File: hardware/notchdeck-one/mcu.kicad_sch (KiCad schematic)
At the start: 10 parts, among them J3 SWD, J4 TC2030_NL, U1 E73-2G4M08S1C

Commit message: Add schematic wiring notes support
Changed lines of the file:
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@@
 		(instances
 			(project "notchdeck-one"
-				(path "/9b1c0f7a-1d2e-4a3b-8c5d-0e6f7a8b9c01/0d4eb303-8502-4a0e-80b0-eb5483675459"
+				(path "/9b1c0f7a-1d2e-4a3b-8c5d-0e6f7a8b9c01/69c9301a-7d1c-4dfc-8a82-adc2c5ab1b11"
 					(reference "U1")
 					(unit 1)
@@
 		(instances
 			(project "notchdeck-one"
-				(path "/9b1c0f7a-1d2e-4a3b-8c5d-0e6f7a8b9c01/0d4eb303-8502-4a0e-80b0-eb5483675459"
+				(path "/9b1c0f7a-1d2e-4a3b-8c5d-0e6f7a8b9c01/69c9301a-7d1c-4dfc-8a82-adc2c5ab1b11"
 					(reference "J3")
 					(unit 1)
@@
 		(instances
 			(project "notchdeck-one"
-				(path "/9b1c0f7a-1d2e-4a3b-8c5d-0e6f7a8b9c01/0d4eb303-8502-4a0e-80b0-eb5483675459"
+				(path "/9b1c0f7a-1d2e-4a3b-8c5d-0e6f7a8b9c01/69c9301a-7d1c-4dfc-8a82-adc2c5ab1b11"
 					(reference "J4")
 					(unit 1)
@@
 		(instances
 			(project "notchdeck-one"
-				(path "/9b1c0f7a-1d2e-4a3b-8c5d-0e6f7a8b9c01/0d4eb303-8502-4a0e-80b0-eb5483675459"
+				(path "/9b1c0f7a-1d2e-4a3b-8c5d-0e6f7a8b9c01/69c9301a-7d1c-4dfc-8a82-adc2c5ab1b11"
 					(reference "C1")
 					(unit 1)
@@
 		(instances
 			(project "notchdeck-one"
-				(path "/9b1c0f7a-1d2e-4a3b-8c5d-0e6f7a8b9c01/0d4eb303-8502-4a0e-80b0-eb5483675459"
+				(path "/9b1c0f7a-1d2e-4a3b-8c5d-0e6f7a8b9c01/69c9301a-7d1c-4dfc-8a82-adc2c5ab1b11"
 					(reference "C2")
 					(unit 1)
@@
 		(instances
 			(project "notchdeck-one"
-				(path "/9b1c0f7a-1d2e-4a3b-8c5d-0e6f7a8b9c01/0d4eb303-8502-4a0e-80b0-eb5483675459"
+				(path "/9b1c0f7a-1d2e-4a3b-8c5d-0e6f7a8b9c01/69c9301a-7d1c-4dfc-8a82-adc2c5ab1b11"
 					(reference "C3")
 					(unit 1)
@@
 		(instances
 			(project "notchdeck-one"
-				(path "/9b1c0f7a-1d2e-4a3b-8c5d-0e6f7a8b9c01/0d4eb303-8502-4a0e-80b0-eb5483675459"
+				(path "/9b1c0f7a-1d2e-4a3b-8c5d-0e6f7a8b9c01/69c9301a-7d1c-4dfc-8a82-adc2c5ab1b11"
 					(reference "C4")
 					(unit 1)
@@
 		(instances
 			(project "notchdeck-one"
-				(path "/9b1c0f7a-1d2e-4a3b-8c5d-0e6f7a8b9c01/0d4eb303-8502-4a0e-80b0-eb5483675459"
+				(path "/9b1c0f7a-1d2e-4a3b-8c5d-0e6f7a8b9c01/69c9301a-7d1c-4dfc-8a82-adc2c5ab1b11"
 					(reference "C5")
 					(unit 1)
@@
 		(instances
 			(project "notchdeck-one"
-				(path "/9b1c0f7a-1d2e-4a3b-8c5d-0e6f7a8b9c01/0d4eb303-8502-4a0e-80b0-eb5483675459"
+				(path "/9b1c0f7a-1d2e-4a3b-8c5d-0e6f7a8b9c01/69c9301a-7d1c-4dfc-8a82-adc2c5ab1b11"
 					(reference "C6")
 					(unit 1)
@@
 		(instances
 			(project "notchdeck-one"
-				(path "/9b1c0f7a-1d2e-4a3b-8c5d-0e6f7a8b9c01/0d4eb303-8502-4a0e-80b0-eb5483675459"
+				(path "/9b1c0f7a-1d2e-4a3b-8c5d-0e6f7a8b9c01/69c9301a-7d1c-4dfc-8a82-adc2c5ab1b11"
 					(reference "SW_RST")
 					(unit 1)
@@
 		)
 	)
-	(text "NotchDeck One — MCU & Programming (U1 Ebyte E73-2G4M08S1C, nRF52840)\nComponents placed, NOT yet wired. Pad numbers = E73 module pads (per notchdeck:E73 symbol / NETPLAN.md).\n\nPOWER:  VDD(19) + VDDH(23) -> +3V3 (tie together = normal-voltage mode; module DC/DC handles REG1).\n        DCCH(25) = NC (leave open). Decouple each VDD/VDDH with 100nF (C1,C2) + 1uF (C3,C4); 10uF bulk (C5) on +3V3.\nUSB:    VBUS(27) -> USB_VBUS(5V)  |  D-(29) -> USB_DM  |  D+(31) -> USB_DP   [from Power sheet, through U7 ESD].\n        nRF on-chip USB regulator + vbus_present() read VBUS directly (no GPIO).\nSWD:    SWDIO(37), SWDCLK(39), nRESET(26/P0.18), +3V3, GND -> wire to BOTH J3 (2x05) and J4 (TC2030-NL) in parallel.\nRESET:  SW_RST: nRESET -> GND (momentary). 100nF (C6) on nRESET. Bootloader double-tap-to-DFU (no BOOT pin).\nFW:     NFC pins P0.09/P0.10 used as GPIO -> set CONFIG_NFCT_PINS_AS_GPIO. nRESET enabled in UICR.\n        P0.00/P0.01 used as GPIO -> LFCLK = internal RC (no 32.768kHz xtal).\n\nE73 full pad map (signal -> net/function):\n 1  P1.11        BTN1 horn-hi (A)        23 VDDH         +3V3 (tie to VDD)\n 2  P1.10        BTN2 horn-lo/bell (B)   24 GND          GND\n 3  P0.03/AIN1   spare (LEVER_S2 alt)    25 DCCH         NC (open)\n 4  P0.28/AIN4   spare (LEVER_S3 alt)    26 P0.18/RESET  nRESET (SW_RST + SWD)\n 5  GND          GND                     27 VBUS         USB_VBUS (5V)\n 6  P1.13        BTN3 door-close (X)     28 P0.15        FG_ALRT  (MAX17048 ALRT)\n 7  P0.02/AIN0   REVERSER_AIN (ADC)      29 USB_D-       USB_DM\n 8  P0.29/AIN5   spare                   30 P0.17        CHG_STAT (MCP73831 STAT)\n 9  P0.31/AIN7   spare                   31 USB_D+       USB_DP\n10  P0.30/AIN6   spare                   32 P0.20        BTN5 ATS-reset (L)\n11  P0.00/XL1    BTN11 (GPIO, no LFXO)   33 P0.13        BTN6 cab/view (R)\n12  P0.26        I2C0_SDA -> AS5600      34 P0.22        HAT_UP\n13  P0.01/XL2    BTN12 (GPIO, no LFXO)   35 P0.24        HAT_DOWN\n14  P0.06        I2C0_SCL -> AS5600      36 P1.00        HAT_LEFT\n15  P0.05/AIN3   spare                   37 SWDIO        SWDIO (J3/J4)\n16  P0.08        WS2812_DIN              38 P1.02        HAT_RIGHT\n17  P1.09        BTN4 door-open (Y)      39 SWDCLK       SWDCLK (J3/J4)\n18  P0.04/AIN2   spare                   40 P1.04        BTN7 select\n19  VDD          +3V3                    41 P0.09/NFC1   BTN9 pantograph\n20  P0.12        I2C1_SDA -> MAX17048    42 P1.06        BTN8 start\n21  GND          GND                     43 P0.10/NFC2   BTN10 headlight\n22  P0.07        I2C1_SCL -> MAX17048"
+	(text "NotchDeck One — MCU & Programming (U1 Ebyte E73-2G4M08S1C, nRF52840)\nComponents placed, NOT yet wired. Pad numbers = E73 module pads (per notchdeck:E73 symbol / NETPLAN.md).\n\nPOWER:  VDD(19) + VDDH(23) -> +3V3 (tie together = normal-voltage mode; module DC/DC handles REG1).\n        DCCH(25) = NC (leave open). Decouple each VDD/VDDH with 100nF (C1,C2) + 1uF (C3,C4); 10uF bulk (C5) on +3V3.\nUSB:    VBUS(27) -> USB_VBUS(5V)  |  D-(29) -> USB_DM  |  D+(31) -> USB_DP   [from Power sheet, through U7 ESD].\n        nRF on-chip USB regulator + vbus_present() read VBUS directly (no GPIO).\nSWD:    SWDIO(37), SWDCLK(39), nRESET(26/P0.18), +3V3, GND -> wire to BOTH J3 (2x05) and J4 (TC2030-NL) in parallel.\nRESET:  SW_RST: nRESET -> GND (momentary). 100nF (C6) on nRESET. Bootloader double-tap-to-DFU (no BOOT pin).\nFW:     NFC pins P0.09/P0.10 used as GPIO -> set CONFIG_NFCT_PINS_AS_GPIO. nRESET enabled in UICR.\n        P0.00/P0.01 used as GPIO -> LFCLK = internal RC (no 32.768kHz xtal).\n\nE73 full pad map (signal -> net/function):\n 1  P1.11        BTN1 horn-hi (A)        23 VDDH         +3V3 (tie to VDD)\n 2  P1.10        BTN2 horn-lo/bell (B)   24 GND          GND\n 3  P0.03/AIN1   LEVER_S0 (coded-sw)     25 DCCH         NC (open)\n 4  P0.28/AIN4   LEVER_S1 (coded-sw)     26 P0.18/RESET  nRESET (SW_RST + SWD)\n 5  GND          GND                     27 VBUS         USB_VBUS (5V)\n 6  P1.13        BTN3 door-close (X)     28 P0.15        FG_ALRT  (MAX17048 ALRT)\n 7  P0.02/AIN0   REVERSER_AIN (ADC)      29 USB_D-       USB_DM\n 8  P0.29/AIN5   spare                   30 P0.17        CHG_STAT (MCP73831 STAT)\n 9  P0.31/AIN7   spare                   31 USB_D+       USB_DP\n10  P0.30/AIN6   spare                   32 P0.20        BTN5 ATS-reset (L)\n11  P0.00/XL1    BTN11 (GPIO, no LFXO)   33 P0.13        BTN6 cab/view (R)\n12  P0.26        I2C0_SDA -> AS5600      34 P0.22        HAT_UP\n13  P0.01/XL2    BTN12 (GPIO, no LFXO)   35 P0.24        HAT_DOWN\n14  P0.06        I2C0_SCL -> AS5600      36 P1.00        HAT_LEFT\n15  P0.05/AIN3   LEVER_S3 (coded-sw)     37 SWDIO        SWDIO (J3/J4)\n16  P0.08        WS2812_DIN              38 P1.02        HAT_RIGHT\n17  P1.09        BTN4 door-open (Y)      39 SWDCLK       SWDCLK (J3/J4)\n18  P0.04/AIN2   LEVER_S2 (coded-sw)     40 P1.04        BTN7 select\n19  VDD          +3V3                    41 P0.09/NFC1   BTN9 pantograph\n20  P0.12        I2C1_SDA -> MAX17048    42 P1.06        BTN8 start\n21  GND          GND                     43 P0.10/NFC2   BTN10 headlight\n22  P0.07        I2C1_SCL -> MAX17048"
 		(exclude_from_sim no)
 		(at 15.00 165.00 0)
-		(effects (font (size 1.5 1.5)) (justify left top))
+		(effects (font (face "Courier New") (size 1.27 1.27)) (justify left top))
 	)
 	(sheet_instances

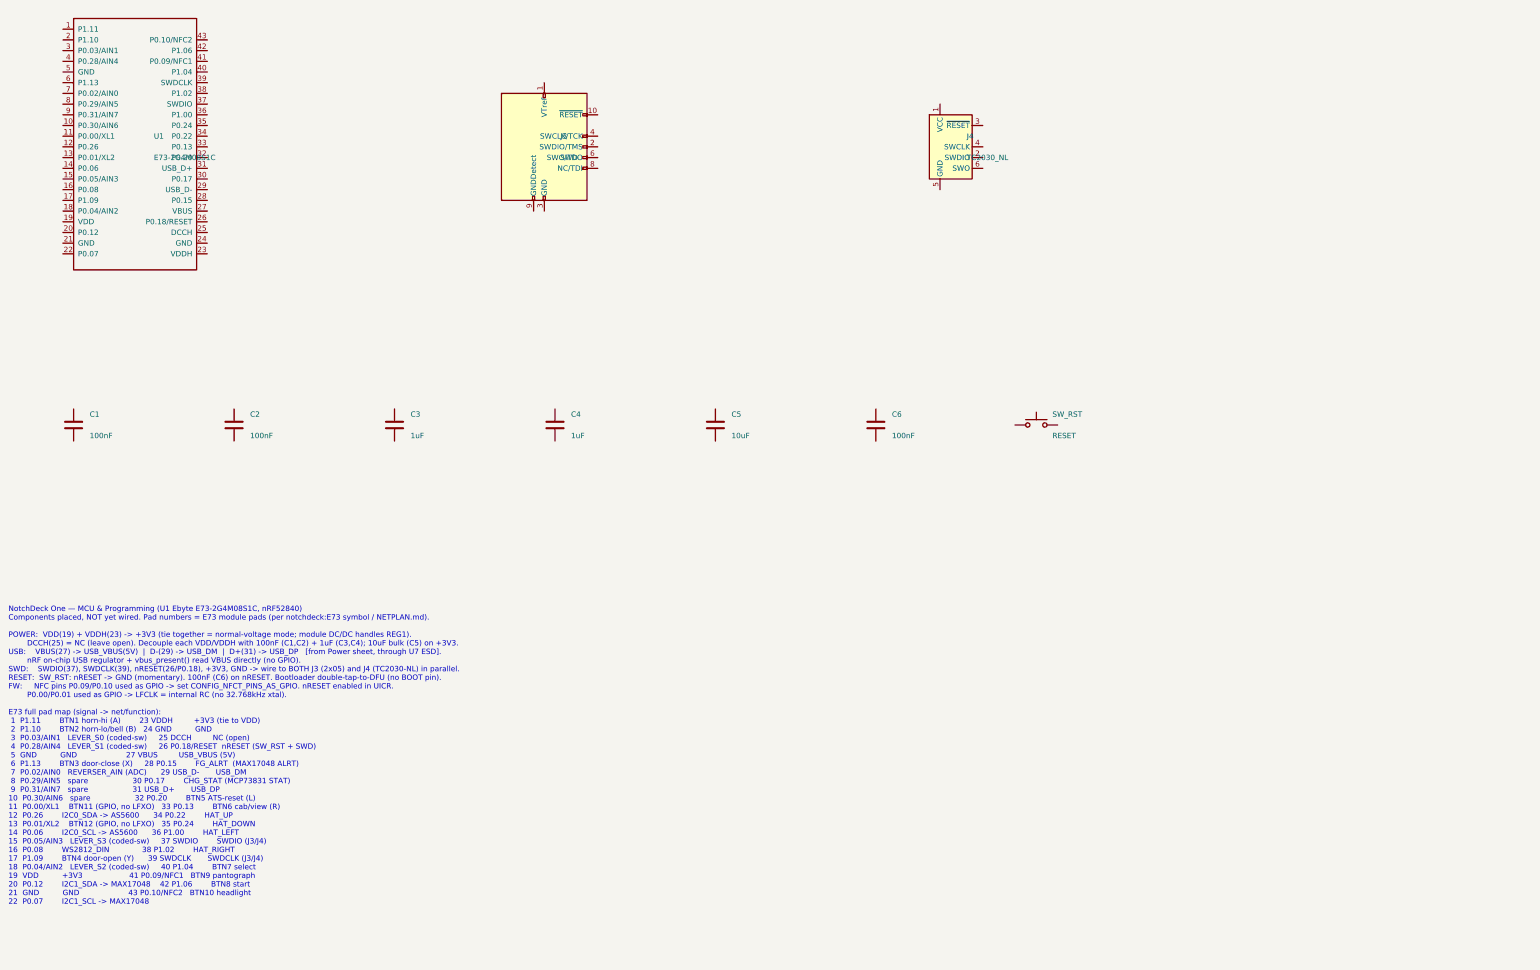
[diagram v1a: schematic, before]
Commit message: Wire and verify NotchDeck controller schematics
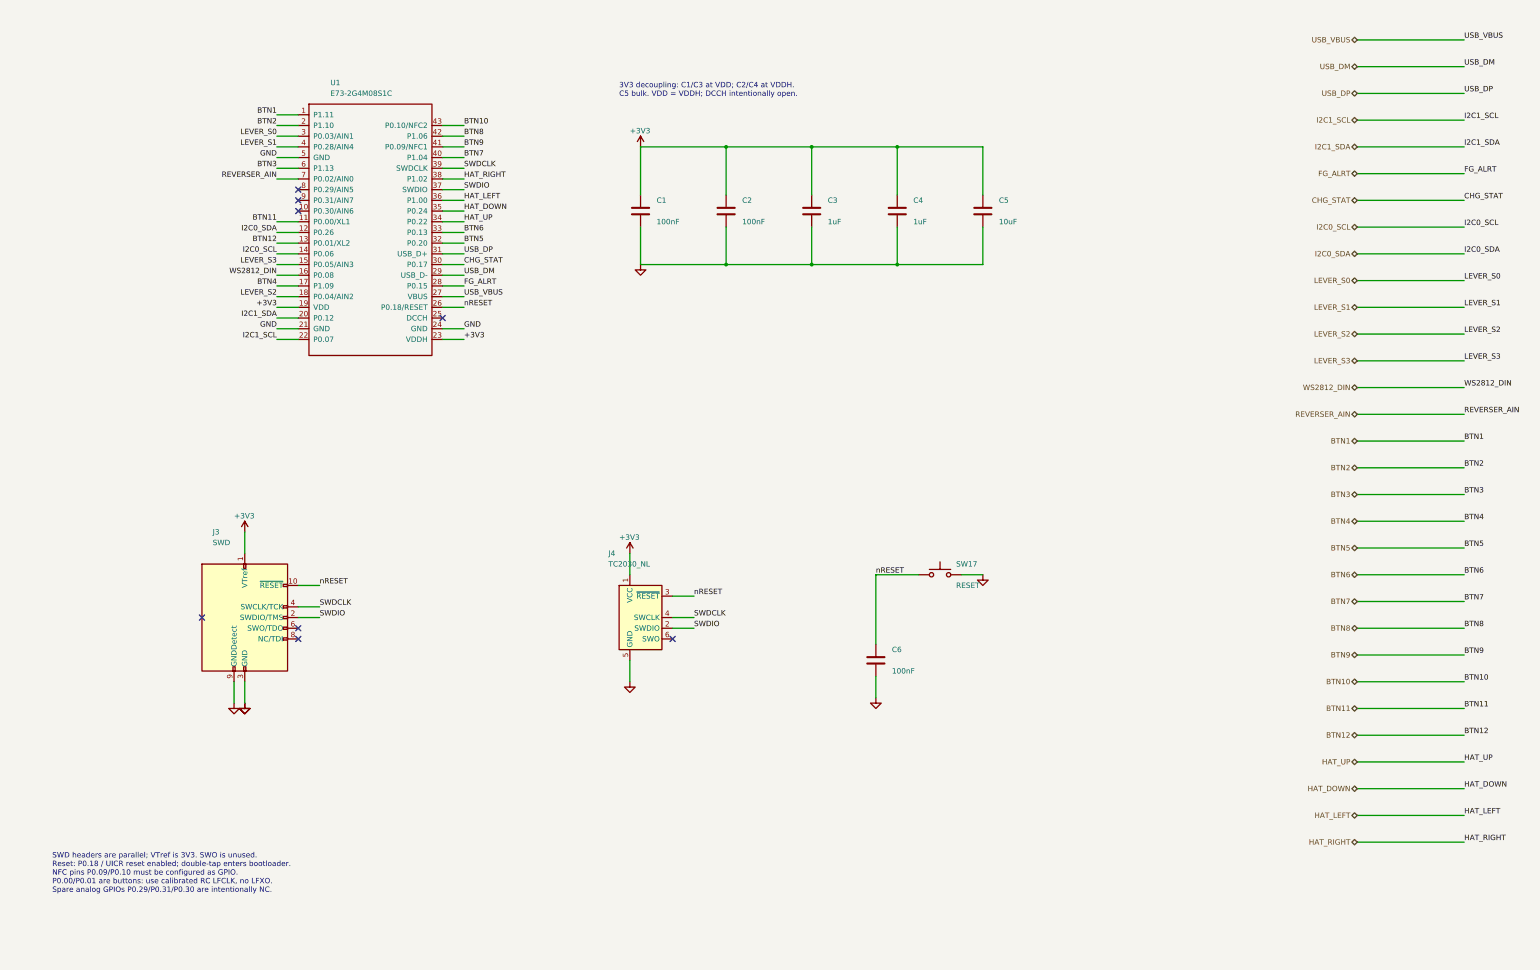
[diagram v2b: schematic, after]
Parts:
- removed J3: SWD, Connector_PinHeader_1.27mm:PinHeader_2x05_P1.27mm_Vertical_SMD, symbol Connector:Conn_ARM_JTAG_SWD_10
- removed J4: TC2030_NL, Connector:Tag-Connect_TC2030-IDC-NL_2x03_P1.27mm_Vertical, symbol Connector:Conn_ARM_SWD_TagConnect_TC2030-NL
- removed SW_RST: RESET, Button_Switch_SMD:SW_Push_1P1T_XKB_TS-1187A, symbol Switch:SW_Push
- added J3: SWD, Connector_PinHeader_1.27mm:PinHeader_2x05_P1.27mm_Vertical_SMD, symbol notchdeck:SWD_2x05
- added J4: TC2030_NL, Connector:Tag-Connect_TC2030-IDC-NL_2x03_P1.27mm_Vertical, symbol notchdeck:SWD_TC2030
- added SW17: RESET, Button_Switch_SMD:SW_Push_1P1T_XKB_TS-1187A, symbol Switch:SW_Push
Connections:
- net +3V3: now reaches C3.1
- net +3V3: now also C1.1, C2.1, C4.1, C5.1, U1.19 (VDD), U1.23 (VDDH), J3.1 (VTref), J4.1 (VCC)
- net GND: now reaches C3.2
- net GND: now also C1.2, C2.2, C4.2, C5.2, C6.2, U1.21 (GND), U1.24 (GND), U1.5 (GND), J3.3 (GND), J3.5 (GND), J3.9 (GNDDetect), J4.5 (GND), SW17.2
- net BTN1: now reaches U1.1 (P1.11)
- net BTN11: now reaches U1.11 (P0.00/XL1)
- net I2C0_SDA: now reaches U1.12 (P0.26)
- net BTN12: now reaches U1.13 (P0.01/XL2)
- net I2C0_SCL: now reaches U1.14 (P0.06)
- net LEVER_S3: now reaches U1.15 (P0.05/AIN3)
- net WS2812_DIN: now reaches U1.16 (P0.08)
- net BTN4: now reaches U1.17 (P1.09)
- net LEVER_S2: now reaches U1.18 (P0.04/AIN2)
- net BTN2: now reaches U1.2 (P1.10)
- net I2C1_SDA: now reaches U1.20 (P0.12)
- net I2C1_SCL: now reaches U1.22 (P0.07)
- net nRESET: now reaches U1.26 (P0.18/RESET)
- net nRESET: now also C6.1, J3.10 (~{RESET}), J4.3 (~{RESET}), SW17.1
- net USB_VBUS: now reaches U1.27 (VBUS)
- net FG_ALRT: now reaches U1.28 (P0.15)
- net USB_DM: now reaches U1.29 (USB_D-)
- net LEVER_S0: now reaches U1.3 (P0.03/AIN1)
- net CHG_STAT: now reaches U1.30 (P0.17)
- net USB_DP: now reaches U1.31 (USB_D+)
- net BTN5: now reaches U1.32 (P0.20)
- net BTN6: now reaches U1.33 (P0.13)
- net HAT_UP: now reaches U1.34 (P0.22)
- net HAT_DOWN: now reaches U1.35 (P0.24)
- net HAT_LEFT: now reaches U1.36 (P1.00)
- net SWDIO: now reaches U1.37 (SWDIO)
- net SWDIO: now also J3.2 (SWDIO/TMS), J4.2 (SWDIO)
- net HAT_RIGHT: now reaches U1.38 (P1.02)
- net SWDCLK: now reaches U1.39 (SWDCLK)
- net SWDCLK: now also J3.4 (SWCLK/TCK), J4.4 (SWCLK)
- net LEVER_S1: now reaches U1.4 (P0.28/AIN4)
- net BTN7: now reaches U1.40 (P1.04)
- net BTN9: now reaches U1.41 (P0.09/NFC1)
- net BTN8: now reaches U1.42 (P1.06)
- net BTN10: now reaches U1.43 (P0.10/NFC2)
- net BTN3: now reaches U1.6 (P1.13)
- net REVERSER_AIN: now reaches U1.7 (P0.02/AIN0)
- no-connect marks 0 -> 8
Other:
- note added: "3V3 decoupling: C1/C3 at VDD; C2/C4 at VDDH. C5 bulk. VDD = VDDH; DCCH intentionally open."
- note added: "SWD headers are parallel; VTref is 3V3. SWO is unused. Reset: P0.18 / UICR reset enabled; double-tap enters bootloader. NFC pins P0.09/P0.10 must be configured as GPIO. P0.00/P0.01 are buttons: use calibrated RC LFCLK, no LFXO. Spare analog GPIOs P0.29/P0.31/P0.30 are intentionally NC."
- note removed: "NotchDeck One — MCU & Programming (U1 Ebyte E73-2G4M08S1C, nRF52840) Components placed, NOT yet wired. Pad numbers = E73 module pads (per notchdeck:E73 symbol / NETPLAN.md). POWER: VDD(19) + VDDH(23) -> +3V3 (tie together = normal-voltage mode; module DC/DC handles REG1). DCCH(25) = NC (leave open). Decouple each VDD/VDDH with 100nF (C1,C2) + 1uF (C3,C4); 10uF bulk (C5) on +3V3. USB: VBUS(27) -> 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"

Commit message: Source controller BOM from JLCPCB and align selected footprints
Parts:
- C1, C2, C6: BOM Checked (none) -> 2026-10-03; BOM Comments (none) -> 100nF 16V X7R ±10% 0402 Multilayer Ceramic Capacitors MLCC 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; JLCPCB Part Type (none) -> Basic; LCSC (none) -> C1525; MPN (none) -> CL05B104KO5NNNC; Manufacturer (none) -> Samsung Electro-Mechanics
- C3, C4: BOM Checked (none) -> 2026-10-03; BOM Comments (none) -> 1uF 25V X5R ±10% 0402 Multilayer Ceramic Capacitors MLCC - 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; JLCPCB Part Type (none) -> Basic; LCSC (none) -> C52923; MPN (none) -> CL05A105KA5NQNC; Manufacturer (none) -> Samsung Electro-Mechanics
- C5: BOM Checked (none) -> 2026-10-03; BOM Comments (none) -> 10uF 25V X5R ±10% 0805 Multilayer Ceramic Capacitors MLCC -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; JLCPCB Part Type (none) -> Basic; LCSC (none) -> C15850; MPN (none) -> CL21A106KAYNNNE; Manufacturer (none) -> Samsung Electro-Mechanics
- J3: footprint Connector_PinHeader_1.27mm:PinHeader_2x05_P1.27mm_Vertical_SMD -> notchdeck:Samtec_FTSH-105-01-L-DV-K; BOM Checked (none) -> 2026-10-03; BOM Comments (none) -> Samtec keyed shroud; manufacturer land pattern. Check JLCPC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; JLCPCB Part Type (none) -> Extended; LCSC (none) -> C448647; MPN (none) -> FTSH-105-01-L-DV-K-TR; Manufacturer (none) -> Samtec
- J4: BOM Comments (none) -> Bare Tag-Connect TC2030-NL PCB contacts; no component to pu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; now left out of the parts list
- SW17: BOM Checked (none) -> 2026-10-03; JLCPCB Part Type (none) -> Basic; LCSC (none) -> C318884; MPN (none) -> TS-1187A-B-A-B; Manufacturer (none) -> XKB Connection
- U1: BOM Checked (none) -> 2026-10-03; BOM Comments (none) -> Ebyte module with onboard antenna; preserve antenna clearan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; JLCPCB Part Type (none) -> Extended
